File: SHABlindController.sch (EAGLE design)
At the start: 34 parts, among them IC1 SPARKCORE, IC2 RAC02-3.3SC, IC3 MOC3042S, IC4 MOC3042S, IC5 RXB1SIL, T1 MOC3042M, T2 MOC3042M

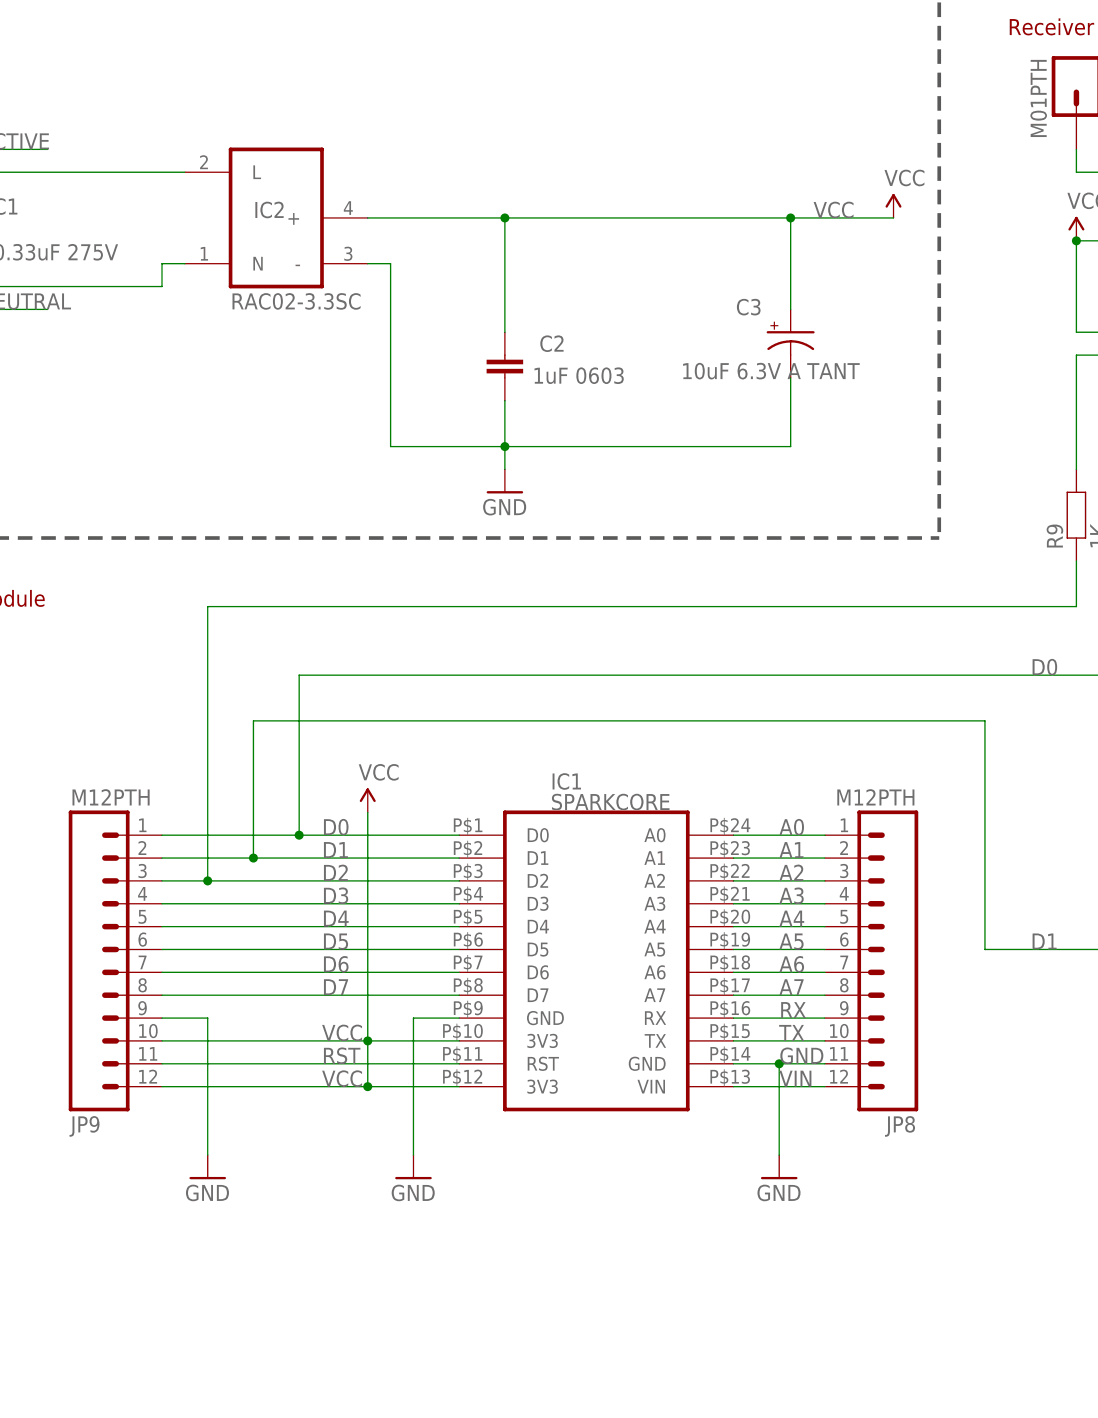
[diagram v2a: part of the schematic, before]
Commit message: Changed power supply from 3.3V to 5V
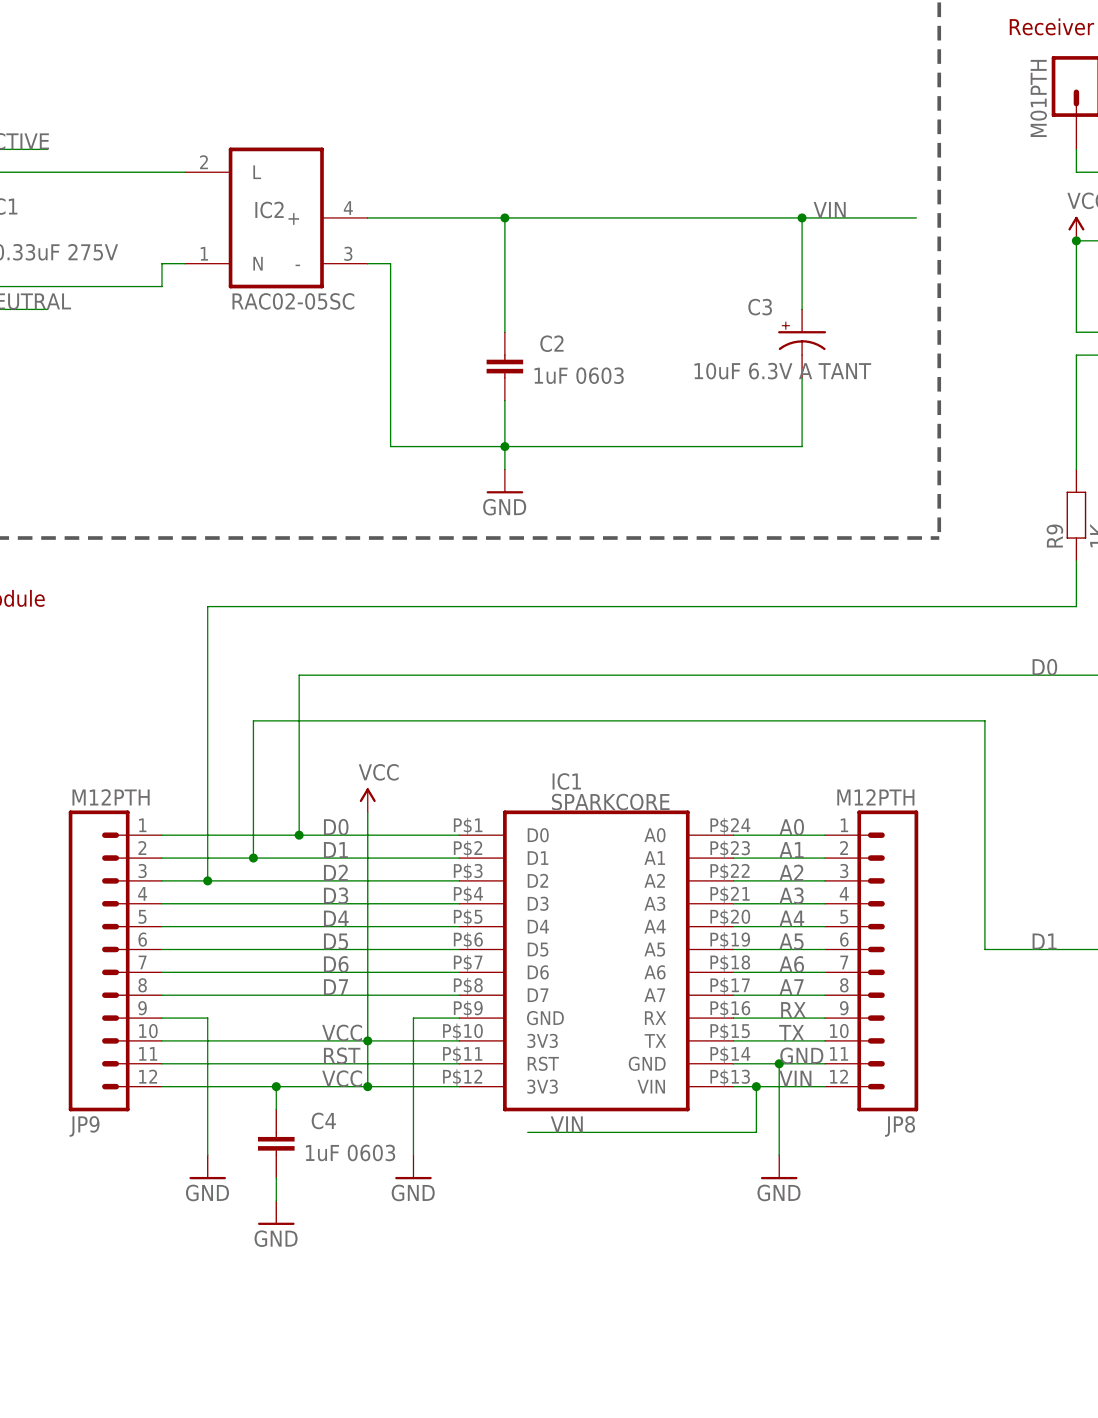
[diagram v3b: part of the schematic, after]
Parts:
- added C4: 1uF 0603, freetronics:CAP0603
- IC2: value RAC02-3.3SC -> RAC02-05SC
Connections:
- net GND: now also C4.2
- net VCC: now also C4.1; no longer C2.1, C3.+, IC2.+
- net VIN: now also C2.1, C3.+, IC2.+
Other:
- moved on the sheet: C3
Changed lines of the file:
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@@
 <part name="C2" library="freetronics" deviceset="CAP" device="0603" value="1uF 0603"/>
 <part name="FID3" library="freetronics" deviceset="FIDUCIAL" device="1X2.5"/>
-<part name="P+5" library="SparkFun" deviceset="VCC" device=""/>
 <part name="T1" library="freetronics-original" deviceset="TRIAC" device="SMD" value="MOC3042M"/>
 <part name="IC3" library="freetronics-jon" deviceset="MOC30*" device="S" technology="42"/>
@@
 <part name="GND4" library="SparkFun" deviceset="GND" device=""/>
 <part name="GND6" library="SparkFun" deviceset="GND" device=""/>
-<part name="IC2" library="freetronics-jon" deviceset="RAC0X-SC" device="" value="RAC02-3.3SC"/>
+<part name="IC2" library="freetronics-jon" deviceset="RAC0X-SC" device="" value="RAC02-05SC"/>
+<part name="C4" library="freetronics" deviceset="CAP" device="0603" value="1uF 0603"/>
+<part name="GND7" library="SparkFun" deviceset="GND" device=""/>
 </parts>
 <sheets>
@@
 <instance part="FID1" gate="G$1" x="20.32" y="22.86"/>
 <instance part="FID2" gate="G$1" x="15.24" y="22.86"/>
-<instance part="C3" gate="G$1" x="110.49" y="137.16" smashed="yes">
-<attribute name="NAME" x="104.394" y="139.065" size="1.778" layer="95"/>
-<attribute name="VALUE" x="98.298" y="131.953" size="1.778" layer="96"/>
+<instance part="C3" gate="G$1" x="111.76" y="137.16" smashed="yes">
+<attribute name="NAME" x="105.664" y="139.065" size="1.778" layer="95"/>
+<attribute name="VALUE" x="99.568" y="131.953" size="1.778" layer="96"/>
 </instance>
 <instance part="C2" gate="G$1" x="78.74" y="132.08" smashed="yes">
@@
 </instance>
 <instance part="FID3" gate="G$1" x="10.16" y="22.86"/>
-<instance part="P+5" gate="1" x="121.92" y="149.86" smashed="yes">
-<attribute name="VALUE" x="120.904" y="153.416" size="1.778" layer="96"/>
-</instance>
 <instance part="T1" gate="G$1" x="203.2" y="91.44" smashed="yes" rot="MR0">
 <attribute name="NAME" x="200.66" y="93.98" size="1.27" layer="95" rot="MR180"/>
@@
 <instance part="GND6" gate="1" x="109.22" y="43.18"/>
 <instance part="IC2" gate="G$1" x="53.34" y="149.86"/>
+<instance part="C4" gate="G$1" x="53.34" y="45.72" smashed="yes">
+<attribute name="NAME" x="57.15" y="48.641" size="1.778" layer="95"/>
+<attribute name="VALUE" x="56.388" y="45.085" size="1.778" layer="96"/>
+</instance>
+<instance part="GND7" gate="1" x="53.34" y="38.1"/>
 </instances>
 <busses>
@@
 <net name="GND" class="0">
 <segment>
-<wire x1="110.49" y1="132.08" x2="110.49" y2="124.46" width="0.1524" layer="91"/>
-<wire x1="78.74" y1="124.46" x2="110.49" y2="124.46" width="0.1524" layer="91"/>
+<wire x1="111.76" y1="132.08" x2="111.76" y2="124.46" width="0.1524" layer="91"/>
+<wire x1="78.74" y1="124.46" x2="111.76" y2="124.46" width="0.1524" layer="91"/>
 <wire x1="78.74" y1="129.54" x2="78.74" y2="124.46" width="0.1524" layer="91"/>
 <wire x1="78.74" y1="124.46" x2="78.74" y2="121.92" width="0.1524" layer="91"/>
@@
 <pinref part="GND3" gate="1" pin="GND"/>
 </segment>
+<segment>
+<pinref part="C4" gate="G$1" pin="2"/>
+<wire x1="53.34" y1="43.18" x2="53.34" y2="40.64" width="0.1524" layer="91"/>
+<pinref part="GND7" gate="1" pin="GND"/>
+</segment>
 </net>
 <net name="VCC" class="1">
-<segment>
-<wire x1="110.49" y1="149.86" x2="121.92" y2="149.86" width="0.1524" layer="91"/>
-<wire x1="110.49" y1="139.7" x2="110.49" y2="149.86" width="0.1524" layer="91"/>
-<junction x="110.49" y="149.86"/>
-<label x="113.03" y="149.86" size="1.778" layer="95"/>
-<pinref part="C3" gate="G$1" pin="+"/>
-<pinref part="P+5" gate="1" pin="VCC"/>
-<pinref part="C2" gate="G$1" pin="1"/>
-<wire x1="78.74" y1="149.86" x2="78.74" y2="137.16" width="0.1524" layer="91"/>
-<wire x1="110.49" y1="149.86" x2="78.74" y2="149.86" width="0.1524" layer="91"/>
-<pinref part="IC2" gate="G$1" pin="+"/>
-<wire x1="78.74" y1="149.86" x2="63.5" y2="149.86" width="0.1524" layer="91"/>
-<junction x="78.74" y="149.86"/>
-</segment>
 <segment>
 <pinref part="IC1" gate="G$1" pin="3V3@1"/>
@@
 <pinref part="P+1" gate="1" pin="VCC"/>
 <pinref part="JP9" gate="G$1" pin="12"/>
-<wire x1="63.5" y1="53.34" x2="40.64" y2="53.34" width="0.1524" layer="91"/>
+<wire x1="63.5" y1="53.34" x2="53.34" y2="53.34" width="0.1524" layer="91"/>
 <junction x="63.5" y="53.34"/>
 <pinref part="JP9" gate="G$1" pin="10"/>
+<wire x1="53.34" y1="53.34" x2="40.64" y2="53.34" width="0.1524" layer="91"/>
 <wire x1="63.5" y1="58.42" x2="40.64" y2="58.42" width="0.1524" layer="91"/>
 <label x="58.42" y="53.34" size="1.778" layer="95"/>
+<pinref part="C4" gate="G$1" pin="1"/>
+<wire x1="53.34" y1="50.8" x2="53.34" y2="53.34" width="0.1524" layer="91"/>
+<junction x="53.34" y="53.34"/>
 </segment>
 <segment>
@@
 <pinref part="JP8" gate="G$1" pin="12"/>
 <pinref part="IC1" gate="G$1" pin="VIN"/>
-<wire x1="114.3" y1="53.34" x2="104.14" y2="53.34" width="0.1524" layer="91"/>
+<wire x1="114.3" y1="53.34" x2="106.68" y2="53.34" width="0.1524" layer="91"/>
 <label x="109.22" y="53.34" size="1.778" layer="95"/>
+<wire x1="106.68" y1="53.34" x2="104.14" y2="53.34" width="0.1524" layer="91"/>
+<wire x1="106.68" y1="53.34" x2="106.68" y2="48.26" width="0.1524" layer="91"/>
+<wire x1="106.68" y1="48.26" x2="81.28" y2="48.26" width="0.1524" layer="91"/>
+<junction x="106.68" y="53.34"/>
+<label x="83.82" y="48.26" size="1.778" layer="95"/>
+</segment>
+<segment>
+<wire x1="111.76" y1="139.7" x2="111.76" y2="149.86" width="0.1524" layer="91"/>
+<label x="113.03" y="149.86" size="1.778" layer="95"/>
+<pinref part="C3" gate="G$1" pin="+"/>
+<pinref part="C2" gate="G$1" pin="1"/>
+<wire x1="78.74" y1="149.86" x2="78.74" y2="137.16" width="0.1524" layer="91"/>
+<wire x1="111.76" y1="149.86" x2="78.74" y2="149.86" width="0.1524" layer="91"/>
+<pinref part="IC2" gate="G$1" pin="+"/>
+<wire x1="78.74" y1="149.86" x2="63.5" y2="149.86" width="0.1524" layer="91"/>
+<junction x="78.74" y="149.86"/>
+<wire x1="124.46" y1="149.86" x2="111.76" y2="149.86" width="0.1524" layer="91"/>
+<junction x="111.76" y="149.86"/>
 </segment>
 </net>
@@
 </sheet>
 </sheets>
-<errors>
-</errors>
 </schematic>
 </drawing>

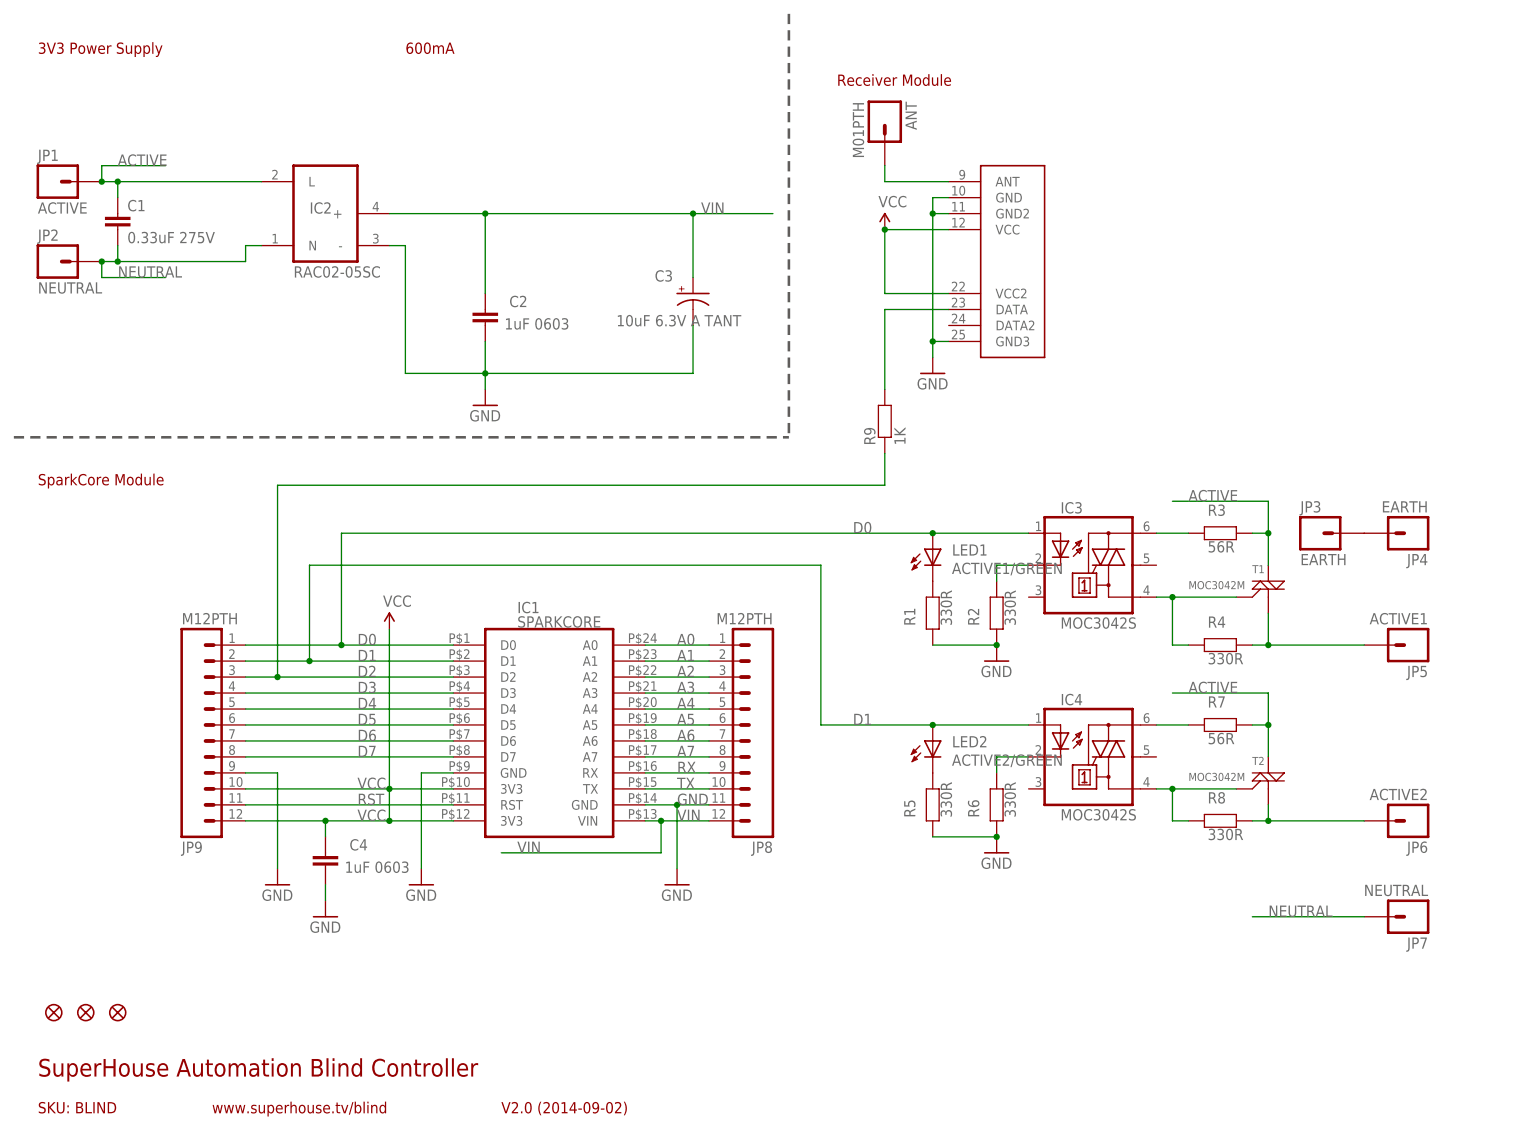
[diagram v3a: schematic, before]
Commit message: Replaced TRIACs with relays; changed power supply to 5V; added piezo
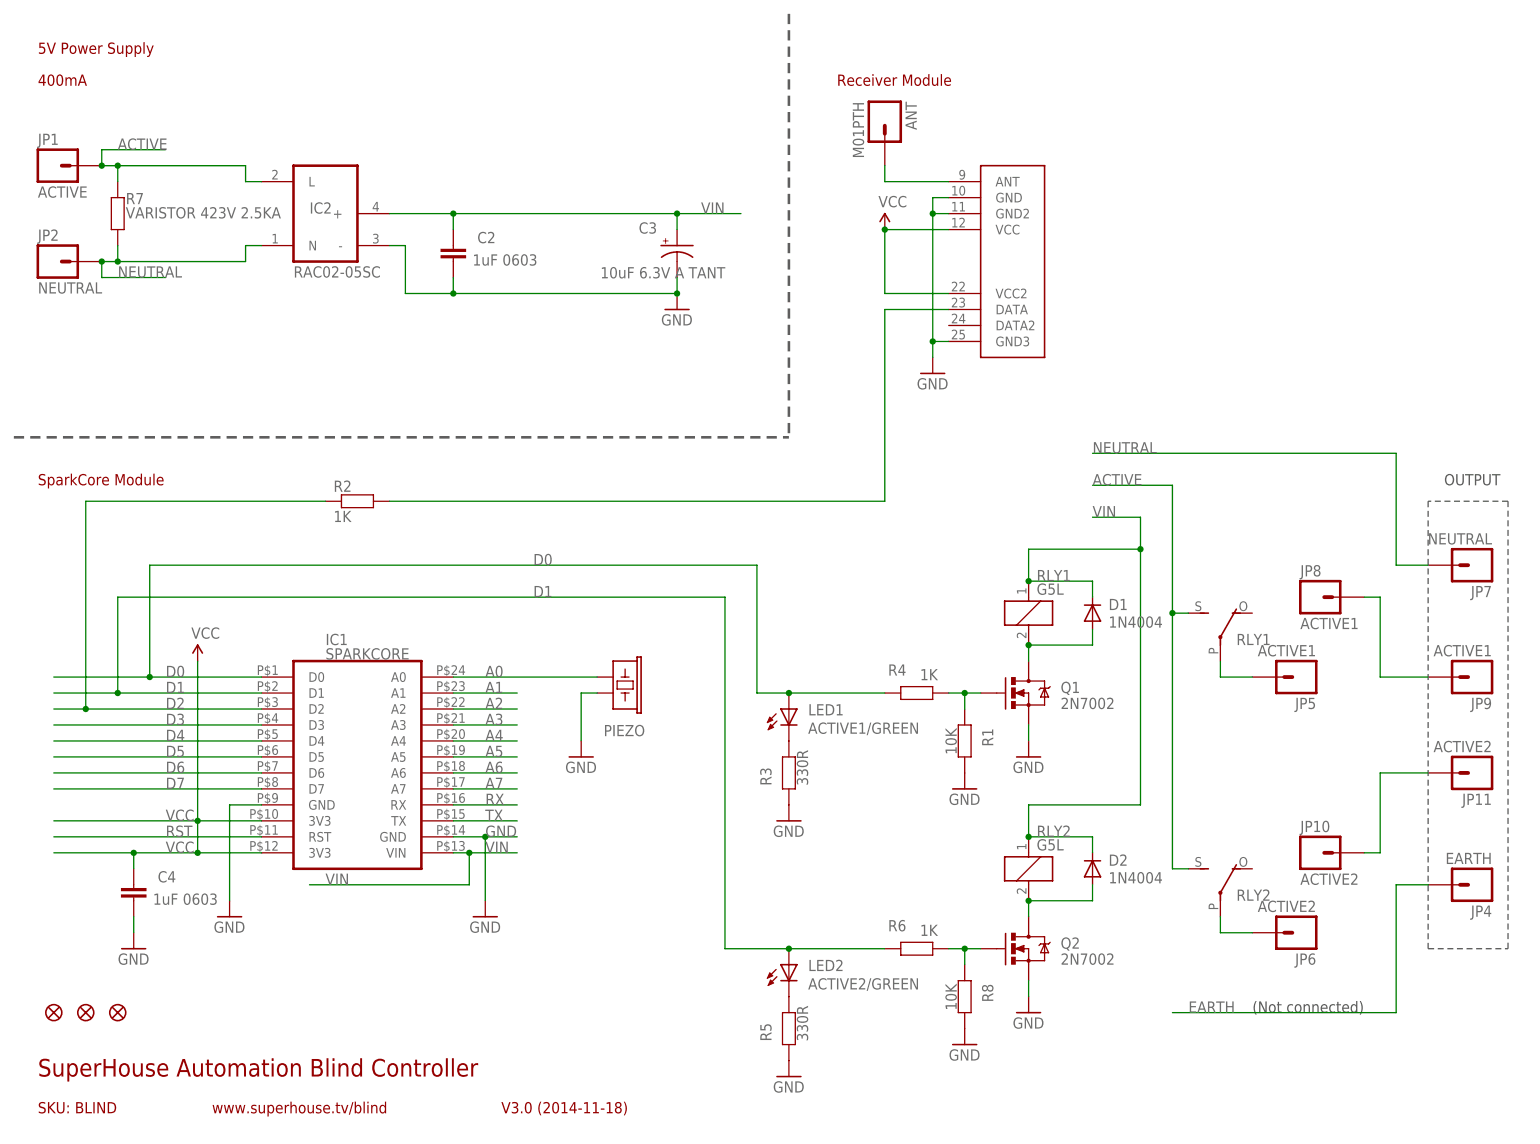
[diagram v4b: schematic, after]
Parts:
- removed C1: 0.33uF 275V, capacitor-wima:C15/9
- removed IC3, IC4: MOC3042S, freetronics-jon:MOC3042S
- removed JP3: EARTH, freetronics-master-v1.1:M01PTH_LARGE
- removed R9: 1K, freetronics:RESISTOR0603
- removed T1, T2: MOC3042M, freetronics-original:TRIACSMD
- added D1, D2: 1N4004, freetronics-master-v1.1:DIODESMB
- added JP10, JP11: ACTIVE2, freetronics-master-v1.1:M01PTH_LARGE
- added PIEZO: BUZZERSMD12X12, freetronics-master-v1:BUZZERSMD12X12
- added Q1, Q2: 2N7002, freetronics-master-v1:MOSFET-NCHANNELSMD
- added RLY1, RLY2: G5L, relay:G5L
- JP8, JP9: value M12PTH -> ACTIVE1; device freetronics-original:M12PTH -> freetronics-master-v1.1:M01PTH_LARGE
- R1, R8: value 330R -> 10K
- R2, R4, R6: value 330R -> 1K
- R3: value 56R -> 330R
- R7: value 56R -> VARISTOR 423V 2.5KA; device freetronics:RESISTOR0603 -> freetronics-master-v1.1:RESISTORPTH1
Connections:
- removed net N$12: IC3.4, R4.1, T1.G
- removed net N$13: IC3.6, R3.1
- removed net N$15: JP3.1, JP4.1
- removed net N$16: IC4.4, R8.1, T2.G
- removed net N$18: IC3.2, R2.2
- removed net N$20: IC4.6, R7.1
- new net EARTH: JP4.1
- new net N$3: D2.A, Q2.D, RLY21.2
- new net N$5: Q1.G, R1.1, R4.1
- new net N$6: Q2.G, R6.1, R8.1
- new net N$7: JP8.1, JP9.1
- new net N$8: JP10.1, JP11.1
- net A0: now also PIEZO.1; no longer JP8.1
- net A1: no longer JP8.2
- net A2: no longer JP8.3
- net A3: no longer JP8.4
- net A4: no longer JP8.5
- net A5: no longer JP8.6
- net A6: no longer JP8.7
- net A7: no longer JP8.8
- net ACTIVE: now also RLY12.S, RLY22.S; no longer C1.1, R3.2, T1.M2, T2.M2
- net D0: now also R4.2; no longer IC3.1, JP9.1
- net D1: now also R6.2; no longer IC4.1, JP9.2
- net D2: now also R2.1; no longer JP9.3, R9.1
- net D3: no longer JP9.4
- net D4: no longer JP9.5
- net D5: no longer JP9.6
- net D6: no longer JP9.7
- net D7: no longer JP9.8
- net GND: now also PIEZO.2, Q1.S, Q2.S, R1.2, R3.1, R8.2; no longer JP8.11, JP9.9, R1.1, R2.1, R6.1
- net N$135: now also R2.2; no longer R9.2
- net N$14: now also RLY12.P; no longer R4.2, T1.M1
- net N$17: now also RLY22.P; no longer R8.2, T2.M1
- net N$25: now also R3.2; no longer R1.2
- net N$4: now also D1.A, Q1.D, RLY11.2; no longer IC4.2, R6.2
- net NEUTRAL: now also R7.1; no longer C1.2
- net RST: no longer JP9.11
- net RX: no longer JP8.9
- net TX: no longer JP8.10
- net VCC: no longer JP9.10, JP9.12
- net VIN: now also D1.C, D2.C, RLY11.1, RLY21.1; no longer JP8.12
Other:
- note added: "(Not connected)"
- note added: "400mA"
- note added: "5V Power Supply"
- note added: "OUTPUT"
- note added: "V3.0 (2014-11-18)"
- note removed: "3V3 Power Supply"
- note removed: "600mA"
- note removed: "V2.0 (2014-09-02)"
- moved on the sheet: C2, C3, C4, IC1, JP1, JP4, JP5, JP6, JP7, LED1, LED2, R1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
